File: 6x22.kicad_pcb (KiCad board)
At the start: 2 copper layers, 418 x 135 mm, 272 parts, among them SW1 RESET, U1 pro_micro, U2 MCP23017, U3 MCP23017

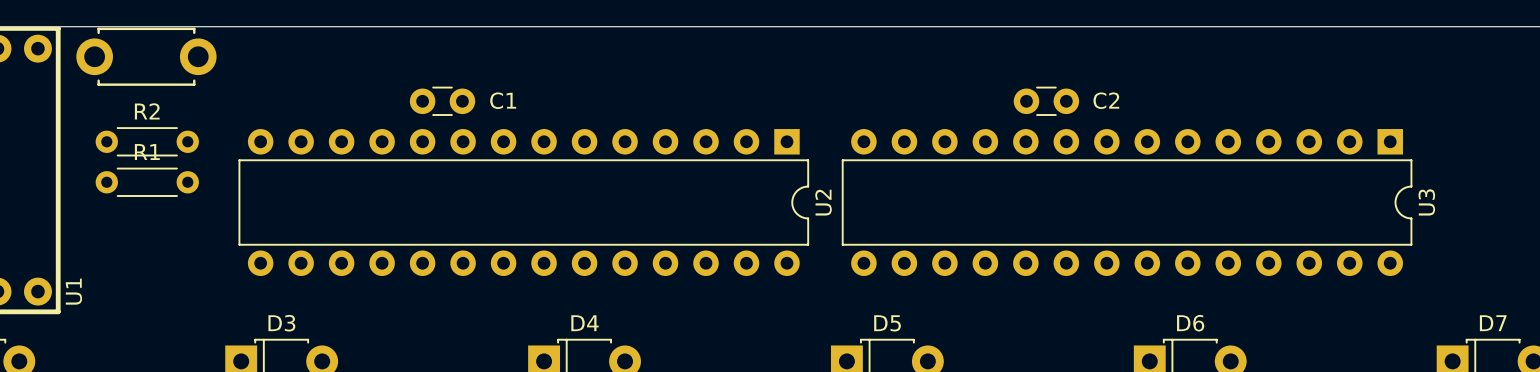
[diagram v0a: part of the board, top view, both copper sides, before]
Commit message: 6x22 with duplex-matrix
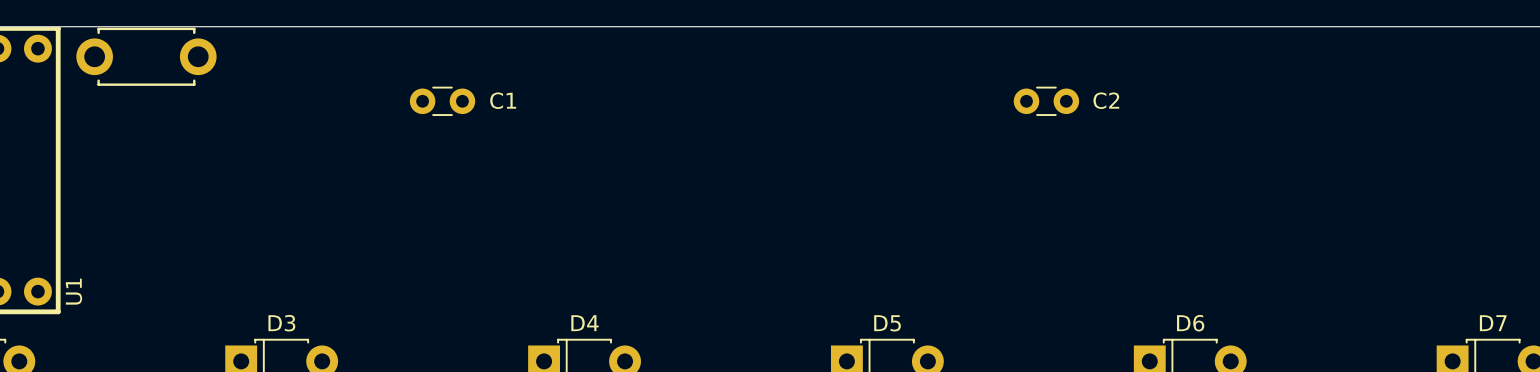
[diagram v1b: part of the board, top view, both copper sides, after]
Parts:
- removed R1, R2: I2C, Resistors_THT:R_Axial_DIN0204_L3.6mm_D1.6mm_P5.08mm_Horizontal
- removed U2, U3: MCP23017, Housings_DIP:DIP-28_W7.62mm
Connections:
- net Net-(U1-Pad10) renamed /LED
- D100 pad 1: /COL4 -> Net-(D100-Pad1)
- D100 pad 2: Net-(D100-Pad2) -> /COL4
- D101 pad 1: /COL4 -> Net-(D101-Pad1)
- D101 pad 2: Net-(D101-Pad2) -> /COL4
- D102 pad 1: /COL4 -> Net-(D102-Pad1)
- D102 pad 2: Net-(D102-Pad2) -> /COL4
- D103 pad 1: /COL4 -> Net-(D103-Pad1)
- D103 pad 2: Net-(D103-Pad2) -> /COL4
- D104 pad 1: /COL4 -> Net-(D104-Pad1)
- D104 pad 2: Net-(D104-Pad2) -> /COL4
- D105 pad 1: /COL4 -> Net-(D105-Pad1)
- D105 pad 2: Net-(D105-Pad2) -> /COL4
- D106 pad 1: /COL4 -> Net-(D106-Pad1)
- D106 pad 2: Net-(D106-Pad2) -> /COL4
- D107 pad 1: /COL4 -> Net-(D107-Pad1)
- D107 pad 2: Net-(D107-Pad2) -> /COL4
- D108 pad 1: /COL4 -> Net-(D108-Pad1)
- D108 pad 2: Net-(D108-Pad2) -> /COL4
- D109 pad 1: /COL4 -> Net-(D109-Pad1)
- D109 pad 2: Net-(D109-Pad2) -> /COL4
- D110 pad 1: /COL4 -> Net-(D110-Pad1)
- D110 pad 2: Net-(D110-Pad2) -> /COL4
- D111 pad 1: Net-(D111-Pad1) -> /COL5
- D112 pad 1: Net-(D111-Pad1) -> /COL5
- D113 pad 1: Net-(D111-Pad1) -> /COL5
- D114 pad 1: Net-(D111-Pad1) -> /COL5
- D115 pad 1: Net-(D111-Pad1) -> /COL5
- D116 pad 1: Net-(D111-Pad1) -> /COL5
- D117 pad 1: Net-(D111-Pad1) -> /COL5
- D118 pad 1: Net-(D111-Pad1) -> /COL5
- D119 pad 1: Net-(D111-Pad1) -> /COL5
- D12 pad 1: /COL0 -> Net-(D12-Pad1)
- D12 pad 2: Net-(D12-Pad2) -> /COL0
- D120 pad 1: Net-(D111-Pad1) -> /COL5
- D121 pad 1: Net-(D111-Pad1) -> /COL5
- D122 pad 1: Net-(D111-Pad1) -> Net-(D122-Pad1)
- D122 pad 2: Net-(D122-Pad2) -> /COL5
- D123 pad 1: Net-(D111-Pad1) -> Net-(D123-Pad1)
- D123 pad 2: Net-(D123-Pad2) -> /COL5
- D124 pad 1: Net-(D111-Pad1) -> Net-(D124-Pad1)
- D124 pad 2: Net-(D124-Pad2) -> /COL5
- D125 pad 1: Net-(D111-Pad1) -> Net-(D125-Pad1)
- D125 pad 2: Net-(D125-Pad2) -> /COL5
- D126 pad 1: Net-(D111-Pad1) -> Net-(D126-Pad1)
- D126 pad 2: Net-(D126-Pad2) -> /COL5
- D127 pad 1: Net-(D111-Pad1) -> Net-(D127-Pad1)
- D127 pad 2: Net-(D127-Pad2) -> /COL5
- D128 pad 1: Net-(D111-Pad1) -> Net-(D128-Pad1)
- D128 pad 2: Net-(D128-Pad2) -> /COL5
- D129 pad 1: Net-(D111-Pad1) -> Net-(D129-Pad1)
- D129 pad 2: Net-(D129-Pad2) -> /COL5
- D13 pad 1: /COL0 -> Net-(D13-Pad1)
- D13 pad 2: Net-(D13-Pad2) -> /COL0
- D130 pad 1: Net-(D111-Pad1) -> Net-(D130-Pad1)
- D130 pad 2: Net-(D130-Pad2) -> /COL5
- D131 pad 1: Net-(D111-Pad1) -> Net-(D131-Pad1)
- D131 pad 2: Net-(D131-Pad2) -> /COL5
- D132 pad 1: Net-(D111-Pad1) -> Net-(D132-Pad1)
- D132 pad 2: Net-(D132-Pad2) -> /COL5
- D14 pad 1: /COL0 -> Net-(D14-Pad1)
- D14 pad 2: Net-(D14-Pad2) -> /COL0
- D15 pad 1: /COL0 -> Net-(D15-Pad1)
- D15 pad 2: Net-(D15-Pad2) -> /COL0
- D16 pad 1: /COL0 -> Net-(D16-Pad1)
- D16 pad 2: Net-(D16-Pad2) -> /COL0
- D17 pad 1: /COL0 -> Net-(D17-Pad1)
- D17 pad 2: Net-(D17-Pad2) -> /COL0
- D18 pad 1: /COL0 -> Net-(D18-Pad1)
- D18 pad 2: Net-(D18-Pad2) -> /COL0
- D19 pad 1: /COL0 -> Net-(D19-Pad1)
- D19 pad 2: Net-(D19-Pad2) -> /COL0
- D20 pad 1: /COL0 -> Net-(D20-Pad1)
- D20 pad 2: Net-(D20-Pad2) -> /COL0
- D21 pad 1: /COL0 -> Net-(D21-Pad1)
- D21 pad 2: Net-(D21-Pad2) -> /COL0
- D22 pad 1: /COL0 -> Net-(D22-Pad1)
- D22 pad 2: Net-(D22-Pad2) -> /COL0
- D34 pad 1: /COL1 -> Net-(D34-Pad1)
- D34 pad 2: Net-(D34-Pad2) -> /COL1
- D35 pad 1: /COL1 -> Net-(D35-Pad1)
- D35 pad 2: Net-(D35-Pad2) -> /COL1
- D36 pad 1: /COL1 -> Net-(D36-Pad1)
- D36 pad 2: Net-(D36-Pad2) -> /COL1
- D37 pad 1: /COL1 -> Net-(D37-Pad1)
- D37 pad 2: Net-(D37-Pad2) -> /COL1
- D38 pad 1: /COL1 -> Net-(D38-Pad1)
- D38 pad 2: Net-(D38-Pad2) -> /COL1
- D39 pad 1: /COL1 -> Net-(D39-Pad1)
- D39 pad 2: Net-(D39-Pad2) -> /COL1
- D40 pad 1: /COL1 -> Net-(D40-Pad1)
- D40 pad 2: Net-(D40-Pad2) -> /COL1
- D41 pad 1: /COL1 -> Net-(D41-Pad1)
- D41 pad 2: Net-(D41-Pad2) -> /COL1
- D42 pad 1: /COL1 -> Net-(D42-Pad1)
- D42 pad 2: Net-(D42-Pad2) -> /COL1
- D43 pad 1: /COL1 -> Net-(D43-Pad1)
- D43 pad 2: Net-(D43-Pad2) -> /COL1
- D44 pad 1: /COL1 -> Net-(D44-Pad1)
- D44 pad 2: Net-(D44-Pad2) -> /COL1
- D56 pad 1: /COL2 -> Net-(D56-Pad1)
- D56 pad 2: Net-(D56-Pad2) -> /COL2
- D57 pad 1: /COL2 -> Net-(D57-Pad1)
- D57 pad 2: Net-(D57-Pad2) -> /COL2
- D58 pad 1: /COL2 -> Net-(D58-Pad1)
- D58 pad 2: Net-(D58-Pad2) -> /COL2
- D59 pad 1: /COL2 -> Net-(D59-Pad1)
- D59 pad 2: Net-(D59-Pad2) -> /COL2
- D60 pad 1: /COL2 -> Net-(D60-Pad1)
- D60 pad 2: Net-(D60-Pad2) -> /COL2
- D61 pad 1: /COL2 -> Net-(D61-Pad1)
- D61 pad 2: Net-(D61-Pad2) -> /COL2
- D62 pad 1: /COL2 -> Net-(D62-Pad1)
- D62 pad 2: Net-(D62-Pad2) -> /COL2
- D63 pad 1: /COL2 -> Net-(D63-Pad1)
- D63 pad 2: Net-(D63-Pad2) -> /COL2
- D64 pad 1: /COL2 -> Net-(D64-Pad1)
- D64 pad 2: Net-(D64-Pad2) -> /COL2
- D65 pad 1: /COL2 -> Net-(D65-Pad1)
- D65 pad 2: Net-(D65-Pad2) -> /COL2
- D66 pad 1: /COL2 -> Net-(D66-Pad1)
- D66 pad 2: Net-(D66-Pad2) -> /COL2
- D78 pad 1: /COL3 -> Net-(D78-Pad1)
- D78 pad 2: Net-(D78-Pad2) -> /COL3
- D79 pad 1: /COL3 -> Net-(D79-Pad1)
- D79 pad 2: Net-(D79-Pad2) -> /COL3
- D80 pad 1: /COL3 -> Net-(D80-Pad1)
- D80 pad 2: Net-(D80-Pad2) -> /COL3
- D81 pad 1: /COL3 -> Net-(D81-Pad1)
- D81 pad 2: Net-(D81-Pad2) -> /COL3
- D82 pad 1: /COL3 -> Net-(D82-Pad1)
- D82 pad 2: Net-(D82-Pad2) -> /COL3
- D83 pad 1: /COL3 -> Net-(D83-Pad1)
- D83 pad 2: Net-(D83-Pad2) -> /COL3
- D84 pad 1: /COL3 -> Net-(D84-Pad1)
- D84 pad 2: Net-(D84-Pad2) -> /COL3
- D85 pad 1: /COL3 -> Net-(D85-Pad1)
- D85 pad 2: Net-(D85-Pad2) -> /COL3
- D86 pad 1: /COL3 -> Net-(D86-Pad1)
- D86 pad 2: Net-(D86-Pad2) -> /COL3
- D87 pad 1: /COL3 -> Net-(D87-Pad1)
- D87 pad 2: Net-(D87-Pad2) -> /COL3
- D88 pad 1: /COL3 -> Net-(D88-Pad1)
- D88 pad 2: Net-(D88-Pad2) -> /COL3
- SW_MX100 pad 1: /ROW11 -> /ROW0
- SW_MX100 pad 2: Net-(D100-Pad2) -> Net-(D100-Pad1)
- SW_MX101 pad 1: /ROW12 -> /ROW1
- SW_MX101 pad 2: Net-(D101-Pad2) -> Net-(D101-Pad1)
- SW_MX102 pad 1: /ROW13 -> /ROW2
- SW_MX102 pad 2: Net-(D102-Pad2) -> Net-(D102-Pad1)
- SW_MX103 pad 1: /ROW14 -> /ROW3
- SW_MX103 pad 2: Net-(D103-Pad2) -> Net-(D103-Pad1)
- SW_MX104 pad 1: /ROW15 -> /ROW4
- SW_MX104 pad 2: Net-(D104-Pad2) -> Net-(D104-Pad1)
- SW_MX105 pad 1: /ROW16 -> /ROW5
- SW_MX105 pad 2: Net-(D105-Pad2) -> Net-(D105-Pad1)
- SW_MX106 pad 1: /ROW17 -> /ROW6
- SW_MX106 pad 2: Net-(D106-Pad2) -> Net-(D106-Pad1)
- SW_MX107 pad 1: /ROW18 -> /ROW7
- SW_MX107 pad 2: Net-(D107-Pad2) -> Net-(D107-Pad1)
- SW_MX108 pad 1: /ROW19 -> /ROW8
- SW_MX108 pad 2: Net-(D108-Pad2) -> Net-(D108-Pad1)
- SW_MX109 pad 1: /ROW20 -> /ROW9
- SW_MX109 pad 2: Net-(D109-Pad2) -> Net-(D109-Pad1)
- SW_MX110 pad 1: /ROW21 -> /ROW10
- SW_MX110 pad 2: Net-(D110-Pad2) -> Net-(D110-Pad1)
- SW_MX12 pad 1: /ROW11 -> /ROW0
- SW_MX12 pad 2: Net-(D12-Pad2) -> Net-(D12-Pad1)
- SW_MX122 pad 1: /ROW11 -> /ROW0
- SW_MX122 pad 2: Net-(D122-Pad2) -> Net-(D122-Pad1)
- SW_MX123 pad 1: /ROW12 -> /ROW1
- SW_MX123 pad 2: Net-(D123-Pad2) -> Net-(D123-Pad1)
- SW_MX124 pad 1: /ROW13 -> /ROW2
- SW_MX124 pad 2: Net-(D124-Pad2) -> Net-(D124-Pad1)
- SW_MX125 pad 1: /ROW14 -> /ROW3
- SW_MX125 pad 2: Net-(D125-Pad2) -> Net-(D125-Pad1)
- SW_MX126 pad 1: /ROW15 -> /ROW4
- SW_MX126 pad 2: Net-(D126-Pad2) -> Net-(D126-Pad1)
- SW_MX127 pad 1: /ROW16 -> /ROW5
- SW_MX127 pad 2: Net-(D127-Pad2) -> Net-(D127-Pad1)
- SW_MX128 pad 1: /ROW17 -> /ROW6
- SW_MX128 pad 2: Net-(D128-Pad2) -> Net-(D128-Pad1)
- SW_MX129 pad 1: /ROW18 -> /ROW7
- SW_MX129 pad 2: Net-(D129-Pad2) -> Net-(D129-Pad1)
- SW_MX13 pad 1: /ROW12 -> /ROW1
- SW_MX13 pad 2: Net-(D13-Pad2) -> Net-(D13-Pad1)
- SW_MX130 pad 1: /ROW19 -> /ROW8
- SW_MX130 pad 2: Net-(D130-Pad2) -> Net-(D130-Pad1)
- SW_MX131 pad 1: /ROW20 -> /ROW9
- SW_MX131 pad 2: Net-(D131-Pad2) -> Net-(D131-Pad1)
- SW_MX132 pad 1: /ROW21 -> /ROW10
- SW_MX132 pad 2: Net-(D132-Pad2) -> Net-(D132-Pad1)
- SW_MX14 pad 1: /ROW13 -> /ROW2
- SW_MX14 pad 2: Net-(D14-Pad2) -> Net-(D14-Pad1)
- SW_MX15 pad 1: /ROW14 -> /ROW3
- SW_MX15 pad 2: Net-(D15-Pad2) -> Net-(D15-Pad1)
- SW_MX16 pad 1: /ROW15 -> /ROW4
- SW_MX16 pad 2: Net-(D16-Pad2) -> Net-(D16-Pad1)
- SW_MX17 pad 1: /ROW16 -> /ROW5
- SW_MX17 pad 2: Net-(D17-Pad2) -> Net-(D17-Pad1)
- SW_MX18 pad 1: /ROW17 -> /ROW6
- SW_MX18 pad 2: Net-(D18-Pad2) -> Net-(D18-Pad1)
- SW_MX19 pad 1: /ROW18 -> /ROW7
- SW_MX19 pad 2: Net-(D19-Pad2) -> Net-(D19-Pad1)
- SW_MX20 pad 1: /ROW19 -> /ROW8
- SW_MX20 pad 2: Net-(D20-Pad2) -> Net-(D20-Pad1)
- SW_MX21 pad 1: /ROW20 -> /ROW9
- SW_MX21 pad 2: Net-(D21-Pad2) -> Net-(D21-Pad1)
- SW_MX22 pad 1: /ROW21 -> /ROW10
- SW_MX22 pad 2: Net-(D22-Pad2) -> Net-(D22-Pad1)
- SW_MX34 pad 1: /ROW11 -> /ROW0
- SW_MX34 pad 2: Net-(D34-Pad2) -> Net-(D34-Pad1)
- SW_MX35 pad 1: /ROW12 -> /ROW1
- SW_MX35 pad 2: Net-(D35-Pad2) -> Net-(D35-Pad1)
- SW_MX36 pad 1: /ROW13 -> /ROW2
- SW_MX36 pad 2: Net-(D36-Pad2) -> Net-(D36-Pad1)
- SW_MX37 pad 1: /ROW14 -> /ROW3
- SW_MX37 pad 2: Net-(D37-Pad2) -> Net-(D37-Pad1)
- SW_MX38 pad 1: /ROW15 -> /ROW4
- SW_MX38 pad 2: Net-(D38-Pad2) -> Net-(D38-Pad1)
- SW_MX39 pad 1: /ROW16 -> /ROW5
- SW_MX39 pad 2: Net-(D39-Pad2) -> Net-(D39-Pad1)
- SW_MX40 pad 1: /ROW17 -> /ROW6
- SW_MX40 pad 2: Net-(D40-Pad2) -> Net-(D40-Pad1)
- SW_MX41 pad 1: /ROW18 -> /ROW7
- SW_MX41 pad 2: Net-(D41-Pad2) -> Net-(D41-Pad1)
- SW_MX42 pad 1: /ROW19 -> /ROW8
- SW_MX42 pad 2: Net-(D42-Pad2) -> Net-(D42-Pad1)
- SW_MX43 pad 1: /ROW20 -> /ROW9
- SW_MX43 pad 2: Net-(D43-Pad2) -> Net-(D43-Pad1)
- SW_MX44 pad 1: /ROW21 -> /ROW10
- SW_MX44 pad 2: Net-(D44-Pad2) -> Net-(D44-Pad1)
- SW_MX56 pad 1: /ROW11 -> /ROW0
- SW_MX56 pad 2: Net-(D56-Pad2) -> Net-(D56-Pad1)
- SW_MX57 pad 1: /ROW12 -> /ROW1
- SW_MX57 pad 2: Net-(D57-Pad2) -> Net-(D57-Pad1)
- SW_MX58 pad 1: /ROW13 -> /ROW2
- SW_MX58 pad 2: Net-(D58-Pad2) -> Net-(D58-Pad1)
- SW_MX59 pad 1: /ROW14 -> /ROW3
- SW_MX59 pad 2: Net-(D59-Pad2) -> Net-(D59-Pad1)
- SW_MX60 pad 1: /ROW15 -> /ROW4
- SW_MX60 pad 2: Net-(D60-Pad2) -> Net-(D60-Pad1)
- SW_MX61 pad 1: /ROW16 -> /ROW5
- SW_MX61 pad 2: Net-(D61-Pad2) -> Net-(D61-Pad1)
- SW_MX62 pad 1: /ROW17 -> /ROW6
- SW_MX62 pad 2: Net-(D62-Pad2) -> Net-(D62-Pad1)
- SW_MX63 pad 1: /ROW18 -> /ROW7
- SW_MX63 pad 2: Net-(D63-Pad2) -> Net-(D63-Pad1)
- SW_MX64 pad 1: /ROW19 -> /ROW8
- SW_MX64 pad 2: Net-(D64-Pad2) -> Net-(D64-Pad1)
- SW_MX65 pad 1: /ROW20 -> /ROW9
- SW_MX65 pad 2: Net-(D65-Pad2) -> Net-(D65-Pad1)
- SW_MX66 pad 1: /ROW21 -> /ROW10
- SW_MX66 pad 2: Net-(D66-Pad2) -> Net-(D66-Pad1)
- SW_MX78 pad 1: /ROW11 -> /ROW0
- SW_MX78 pad 2: Net-(D78-Pad2) -> Net-(D78-Pad1)
- SW_MX79 pad 1: /ROW12 -> /ROW1
- SW_MX79 pad 2: Net-(D79-Pad2) -> Net-(D79-Pad1)
- SW_MX80 pad 1: /ROW13 -> /ROW2
- SW_MX80 pad 2: Net-(D80-Pad2) -> Net-(D80-Pad1)
- SW_MX81 pad 1: /ROW14 -> /ROW3
- SW_MX81 pad 2: Net-(D81-Pad2) -> Net-(D81-Pad1)
- SW_MX82 pad 1: /ROW15 -> /ROW4
- SW_MX82 pad 2: Net-(D82-Pad2) -> Net-(D82-Pad1)
- SW_MX83 pad 1: /ROW16 -> /ROW5
- SW_MX83 pad 2: Net-(D83-Pad2) -> Net-(D83-Pad1)
- SW_MX84 pad 1: /ROW17 -> /ROW6
- SW_MX84 pad 2: Net-(D84-Pad2) -> Net-(D84-Pad1)
- SW_MX85 pad 1: /ROW18 -> /ROW7
- SW_MX85 pad 2: Net-(D85-Pad2) -> Net-(D85-Pad1)
- SW_MX86 pad 1: /ROW19 -> /ROW8
- SW_MX86 pad 2: Net-(D86-Pad2) -> Net-(D86-Pad1)
- SW_MX87 pad 1: /ROW20 -> /ROW9
- SW_MX87 pad 2: Net-(D87-Pad2) -> Net-(D87-Pad1)
- SW_MX88 pad 1: /ROW21 -> /ROW10
- SW_MX88 pad 2: Net-(D88-Pad2) -> Net-(D88-Pad1)
- U1 pad 1: Net-(U1-Pad1) -> /ROW0
- U1 pad 11: Net-(U1-Pad11) -> /COL0
- U1 pad 12: Net-(U1-Pad12) -> /COL1
- U1 pad 13: /COL5 -> /COL2
- U1 pad 14: /COL4 -> /COL3
- U1 pad 15: /COL3 -> /COL4
- U1 pad 16: /COL2 -> /COL5
- U1 pad 17: /COL1 -> /ROW7
- U1 pad 18: /COL0 -> /ROW8
- U1 pad 19: Net-(U1-Pad19) -> /ROW9
- U1 pad 2: Net-(U1-Pad2) -> /ROW1
- U1 pad 20: Net-(U1-Pad20) -> /ROW10
- U1 pad 5: Net-(R2-Pad2) -> /ROW2
- U1 pad 6: Net-(R1-Pad2) -> /ROW3
- U1 pad 7: Net-(U1-Pad7) -> /ROW4
- U1 pad 8: Net-(U1-Pad8) -> /ROW5
- U1 pad 9: Net-(U1-Pad9) -> /ROW6
